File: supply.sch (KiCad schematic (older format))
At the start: 91 parts, among them IC12 74HC00PW, IC13 SN74LVC1G126DCKR, IC4 TPS7A0518PDBVT, J12 533980471, T3 BSS138APW, U1 LM3671MF-1.5_NOPB, U2 LM62440-Q1, U3 SN74LXC1T45DBVR, U5 LM3671MF-1.5_NOPB, U6 SIC477ED-T1-GE3

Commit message: Save current status
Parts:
- added C? (x2): C_100n_0402, jetson-nano-baseboard-footprints:0402-cap, symbol jetson-nano-baseboard:C_100n_0402
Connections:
- net 1V8_SYS: now also C?.2
- net 5V0_SYS: now also C?.2
- net GND: now also C?.1, C?.1
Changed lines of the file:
@@
 	0    1    1    0
 $EndComp
+$Comp
+L jetson-nano-baseboard:C_100n_0402 C?
+U 1 1 61D57528
+P 14800 6750
+F 0 "C?" H 14685 6705 60  0000 R CNN
+F 1 "C_100n_0402" H 14800 6600 60  0001 C CNN
+F 2 "jetson-nano-baseboard-footprints:0402-cap" H 15000 6950 60  0001 L CNN
+F 3 "" H 14800 6750 50  0001 C CNN
+F 4 "Walsin" H 15000 7150 60  0001 L CNN "Manufacturer"
+F 5 "0402X104K6R3CT" H 15000 7050 60  0001 L CNN "MPN"
+F 6 "100n" H 14685 6803 50  0000 R CNN "Val"
+	1    14800 6750
+	-1   0    0    1
+$EndComp
+Text GLabel 14800 6600 2    50   Input ~ 0
+5V0_SYS
+$Comp
+L jetson-nano-baseboard:GND #GND_?
+U 1 1 61D7CDF9
+P 14800 6900
+F 0 "#GND_?" H 14800 6900 20  0001 C CNN
+F 1 "GND" H 14803 6757 30  0000 C CNN
+F 2 "" H 14800 6900 70  0001 C CNN
+F 3 "" H 14800 6900 70  0001 C CNN
+	1    14800 6900
+	1    0    0    -1
+$EndComp
+$Comp
+L jetson-nano-baseboard:C_100n_0402 C?
+U 1 1 61D9041A
+P 12350 6775
+F 0 "C?" H 12235 6730 60  0000 R CNN
+F 1 "C_100n_0402" H 12350 6625 60  0001 C CNN
+F 2 "jetson-nano-baseboard-footprints:0402-cap" H 12550 6975 60  0001 L CNN
+F 3 "" H 12350 6775 50  0001 C CNN
+F 4 "Walsin" H 12550 7175 60  0001 L CNN "Manufacturer"
+F 5 "0402X104K6R3CT" H 12550 7075 60  0001 L CNN "MPN"
+F 6 "100n" H 12235 6828 50  0000 R CNN "Val"
+	1    12350 6775
+	1    0    0    1
+$EndComp
+$Comp
+L jetson-nano-baseboard:GND #GND_?
+U 1 1 61D90421
+P 12350 6925
+F 0 "#GND_?" H 12350 6925 20  0001 C CNN
+F 1 "GND" H 12353 6782 30  0000 C CNN
+F 2 "" H 12350 6925 70  0001 C CNN
+F 3 "" H 12350 6925 70  0001 C CNN
+	1    12350 6925
+	-1   0    0    -1
+$EndComp
+Text GLabel 12350 6625 0    50   Input ~ 0
+1V8_SYS
 $EndSCHEMATC

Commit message: Finish routing, cleanup silks
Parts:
- gave numbers to parts that had none: 2
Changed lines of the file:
@@
 $EndComp
 $Comp
-L jetson-nano-baseboard:C_100n_0402 C?
+L jetson-nano-baseboard:C_100n_0402 C88
 U 1 1 61D57528
 P 14800 6750
-F 0 "C?" H 14685 6705 60  0000 R CNN
+F 0 "C88" H 14685 6705 60  0000 R CNN
 F 1 "C_100n_0402" H 14800 6600 60  0001 C CNN
 F 2 "jetson-nano-baseboard-footprints:0402-cap" H 15000 6950 60  0001 L CNN
@@
 5V0_SYS
 $Comp
-L jetson-nano-baseboard:GND #GND_?
+L jetson-nano-baseboard:GND #GND_0165
 U 1 1 61D7CDF9
 P 14800 6900
-F 0 "#GND_?" H 14800 6900 20  0001 C CNN
+F 0 "#GND_0165" H 14800 6900 20  0001 C CNN
 F 1 "GND" H 14803 6757 30  0000 C CNN
 F 2 "" H 14800 6900 70  0001 C CNN
@@
 $EndComp
 $Comp
-L jetson-nano-baseboard:C_100n_0402 C?
+L jetson-nano-baseboard:C_100n_0402 C86
 U 1 1 61D9041A
 P 12350 6775
-F 0 "C?" H 12235 6730 60  0000 R CNN
+F 0 "C86" H 12235 6730 60  0000 R CNN
 F 1 "C_100n_0402" H 12350 6625 60  0001 C CNN
 F 2 "jetson-nano-baseboard-footprints:0402-cap" H 12550 6975 60  0001 L CNN
@@
 $EndComp
 $Comp
-L jetson-nano-baseboard:GND #GND_?
+L jetson-nano-baseboard:GND #GND_0166
 U 1 1 61D90421
 P 12350 6925
-F 0 "#GND_?" H 12350 6925 20  0001 C CNN
+F 0 "#GND_0166" H 12350 6925 20  0001 C CNN
 F 1 "GND" H 12353 6782 30  0000 C CNN
 F 2 "" H 12350 6925 70  0001 C CNN

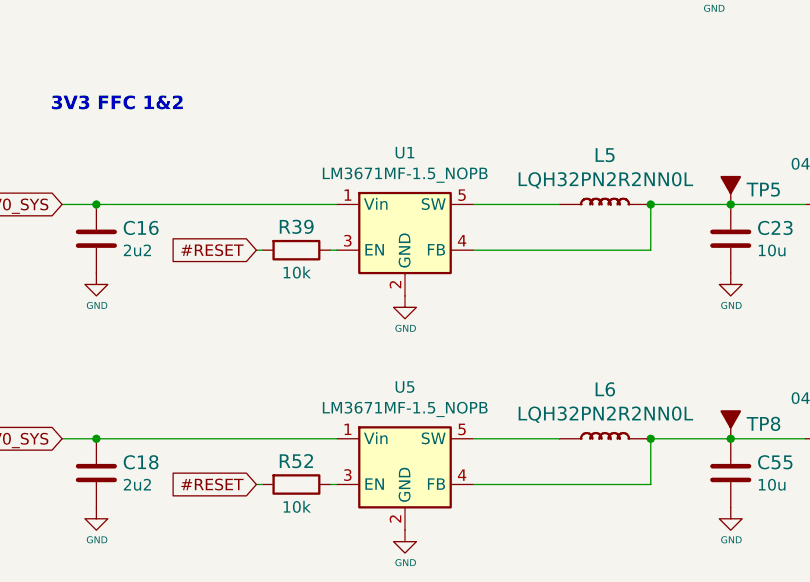
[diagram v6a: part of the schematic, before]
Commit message: Update MPN of U1 and U5 to LM3671MF-3.3/NOPB
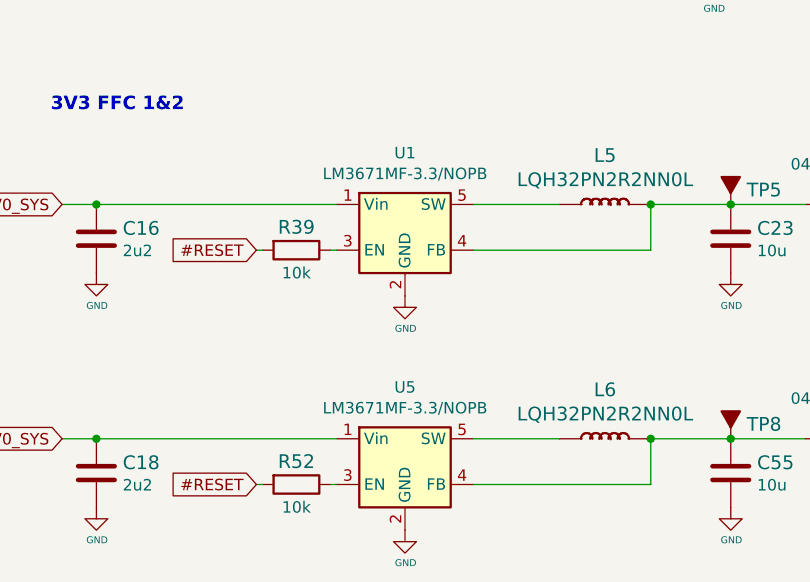
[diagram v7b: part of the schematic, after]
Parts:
- U1, U5: value LM3671MF-1.5_NOPB -> LM3671MF-3.3/NOPB; MPN LM3671MF-1.5/NOPB -> LM3671MF-3.3/NOPB
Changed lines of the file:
@@
 P 2575 7925
 F 0 "U1" H 2575 8250 50  0000 C CNN
-F 1 "LM3671MF-1.5_NOPB" H 2575 8159 50  0000 C CNN
+F 1 "LM3671MF-3.3/NOPB" H 2575 8159 50  0000 C CNN
 F 2 "jetson-nano-baseboard-footprints:SOT-23-5" H 2625 7675 50  0001 L CNN
 F 3 "" H 2325 7575 50  0001 C CNN
-F 4 "LM3671MF-1.5/NOPB" H 2575 7925 50  0001 C CNN "MPN"
+F 4 "LM3671MF-3.3/NOPB" H 2575 7925 50  0001 C CNN "MPN"
 F 5 "Texas Instruments" H 2575 7925 50  0001 C CNN "Manufacturer"
 	1    2575 7925
@@
 P 2575 8950
 F 0 "U5" H 2575 9275 50  0000 C CNN
-F 1 "LM3671MF-1.5_NOPB" H 2575 9184 50  0000 C CNN
+F 1 "LM3671MF-3.3/NOPB" H 2575 9184 50  0000 C CNN
 F 2 "jetson-nano-baseboard-footprints:SOT-23-5" H 2625 8700 50  0001 L CNN
 F 3 "" H 2325 8600 50  0001 C CNN
-F 4 "LM3671MF-1.5/NOPB" H 2575 8950 50  0001 C CNN "MPN"
+F 4 "LM3671MF-3.3/NOPB" H 2575 8950 50  0001 C CNN "MPN"
 F 5 "Texas Instruments" H 2575 8950 50  0001 C CNN "Manufacturer"
 	1    2575 8950

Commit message: Change XFL4015-122MEC XFL4020-222MEC
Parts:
- L1: value XFL4015-122MEC -> XFL4020-222MEC; symbol jetson-nano-baseboard:XFL4015-122MEC -> jetson-nano-baseboard:XFL4020-222MEC; MPN XFL4015-122MEC -> XFL4020-222MEC; MaxCur 7.1A -> 6A; Val 1u2/7.1A -> 2u2/3.7A
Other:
- note added: "3V3/3.5A\n"
- note removed: "3V3/4A"
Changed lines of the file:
@@
 3V3 DC/DC
 Text Notes 900  4750 0    59   ~ 12
-3V3/4A
+3V3/3.5A\n
 Wire Wire Line
 	3325 5475 3325 5375
@@
 Connection ~ 4625 5675
 $Comp
-L jetson-nano-baseboard:XFL4015-122MEC L1
+L jetson-nano-baseboard:XFL4020-222MEC L1
 U 1 1 62296CEC
 P 5400 5675
 F 0 "L1" H 5400 5364 60  0000 C CNN
-F 1 "XFL4015-122MEC" H 5400 5470 60  0000 C CNN
+F 1 "XFL4020-222MEC" H 5400 5470 60  0000 C CNN
 F 2 "jetson-nano-baseboard-footprints:XFL4015-122MEC" H 5450 6100 60  0001 L CNN
 F 3 "" H 5600 5975 60  0001 L CNN
-F 4 "XFL4015-122MEC" H 5450 6400 60  0001 L CNN "MPN"
+F 4 "XFL4020-222MEC" H 5450 6400 60  0001 L CNN "MPN"
 F 5 "Coilcraft" H 5450 6500 60  0001 L CNN "Manufacturer"
-F 6 "7.1A" H 5550 6300 50  0001 C CNN "MaxCur"
+F 6 "6A" H 5550 6300 50  0001 C CNN "MaxCur"
 F 7 "4.3x4.3" H 5600 6200 50  0001 C CNN "Size"
-F 8 "1u2/7.1A" H 5400 5568 50  0000 C CNN "Val"
+F 8 "2u2/3.7A" H 5400 5568 50  0000 C CNN "Val"
 	1    5400 5675
 	-1   0    0    1
